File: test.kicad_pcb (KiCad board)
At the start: 2 copper layers, 56.7 x 86.9 mm, 6 parts, among them J1 Conn_01x02_Female, J2 Conn_01x02_Female, J3 DB9_Male, J4 Conn_01x02_Female, J5 Conn_01x02_Female, U1 MCP2551-I-SN

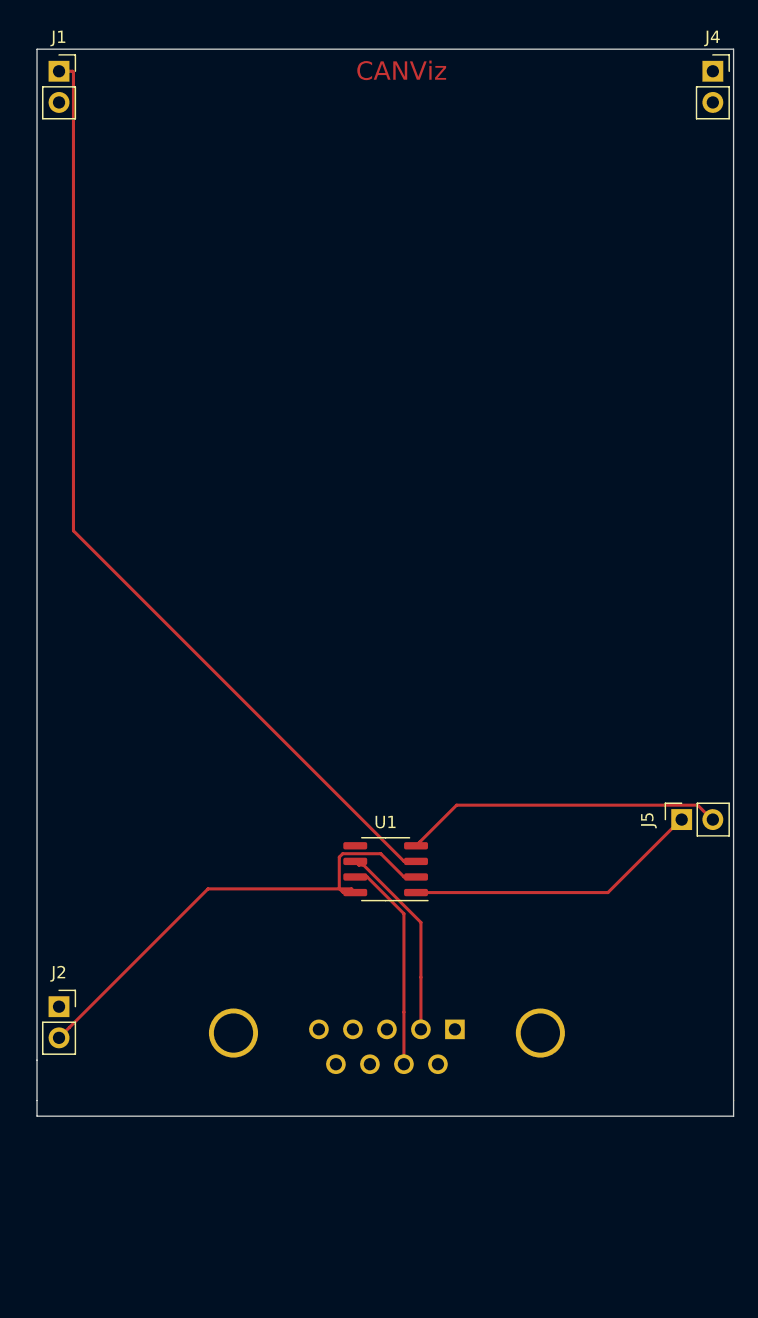
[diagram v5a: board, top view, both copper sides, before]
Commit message: regular mcp2551
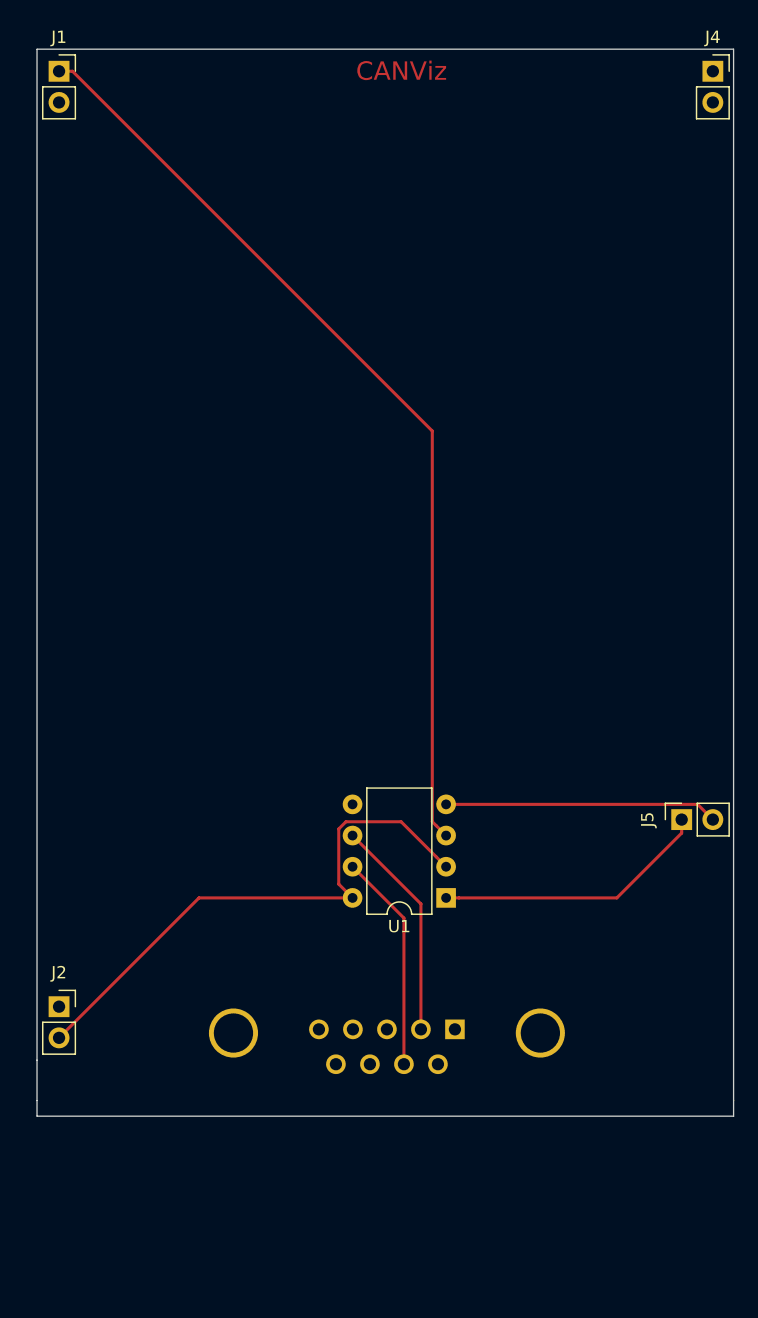
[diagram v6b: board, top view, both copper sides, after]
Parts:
- U1: value MCP2551-I-SN -> MCP2551-I-P; footprint Package_SO:SOIC-8_3.9x4.9mm_P1.27mm -> Package_DIP:DIP-8_W7.62mm
- moved U1 5.45 mm to (87.6, 129.5)
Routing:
- net GND_STM: track 40.4 -> 45.2 mm
- net PB12: track 26.0 -> 22.2 mm
- net canL: track 16.1 -> 18.1 mm
- net +5V_STM: track 77.6 -> 76.0 mm
- net PB13: track 24.0 -> 22.5 mm
